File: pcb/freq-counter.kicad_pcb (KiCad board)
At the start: 4 copper layers, 152.4 x 167.6 mm, 107 parts, among them J1 RPM on board, J10 Power_T1, J11 Hz/RPM_Terminal1, J12 Hz/RPM_Terminal0, J13 1kMG_Terminal1, J14 1kMG_Terminal0, J2 BNC, J3 RPM to Board, J4 Jack-DC, J5 Segments-Terminal0, J6 Digits-Terminal0, J7 Segments-Terminal1, J8 Digits-Terminal1, J9 Power_Terminal1, Q1 CSC388A, Q10 2SC1815, Q11 2SC1815, Q12 2SC1815, Q13 2SC1815, Q14 2SC1815, Q2 CSC388A, Q3 2SA1015, Q4 2SC1815, Q5 2SC1815, Q6 CSC388A, Q7 CSC388A, Q8 CSC388A, Q9 2SC1815, SW1 on/off, SW2 count up, SW3 toggle, SW4 SW_SIGNAL, U1 SN74HC02N, U2 ATTINY4313-PU(freq-counter), U3 EE-SX460, U4 74HC00, U5 74HC00, U6 74HC00, U7 7seg-2digit-ca, U8 7seg-2digit-ca, U9 7seg-2digit-ca, Y1 10MHz

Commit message: LED に関してのCvPcbをやり直した。
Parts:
- D1, D10, D2, D3, D4, D5, D6, D7, D8, D9: footprint LEDs:LED_D5.0mm -> LED_THT:LED_D5.0mm

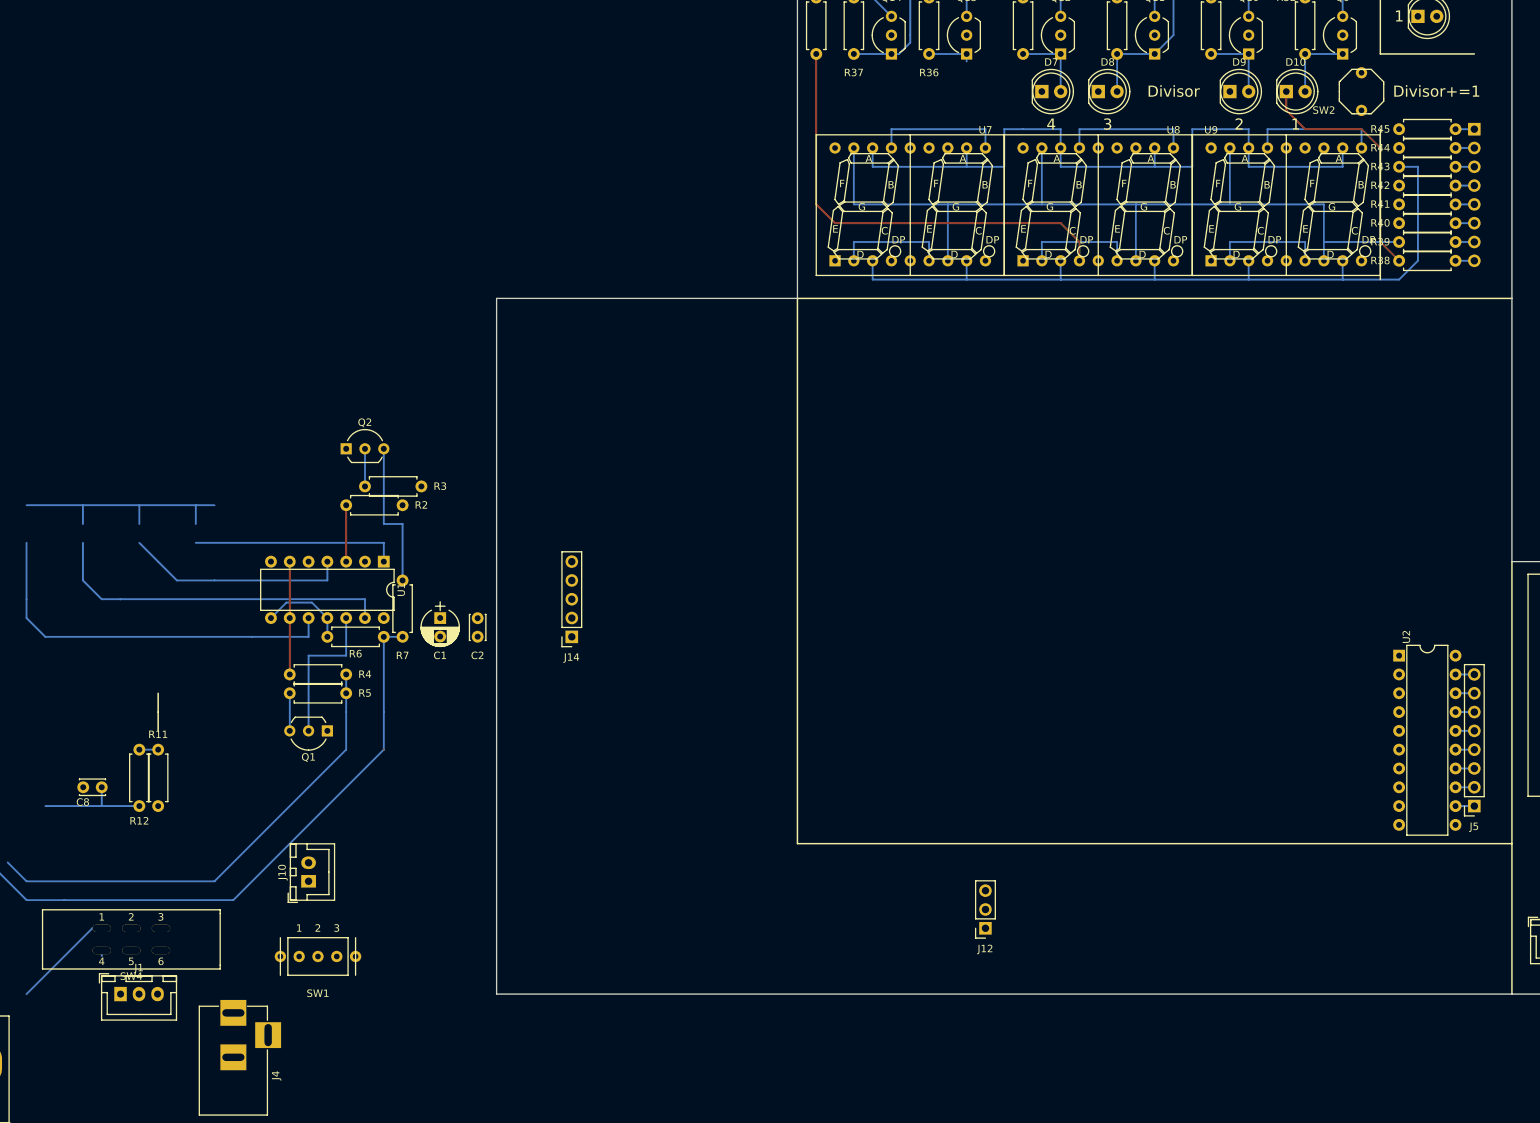
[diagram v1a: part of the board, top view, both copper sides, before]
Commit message: count-up を Terminal 化した。
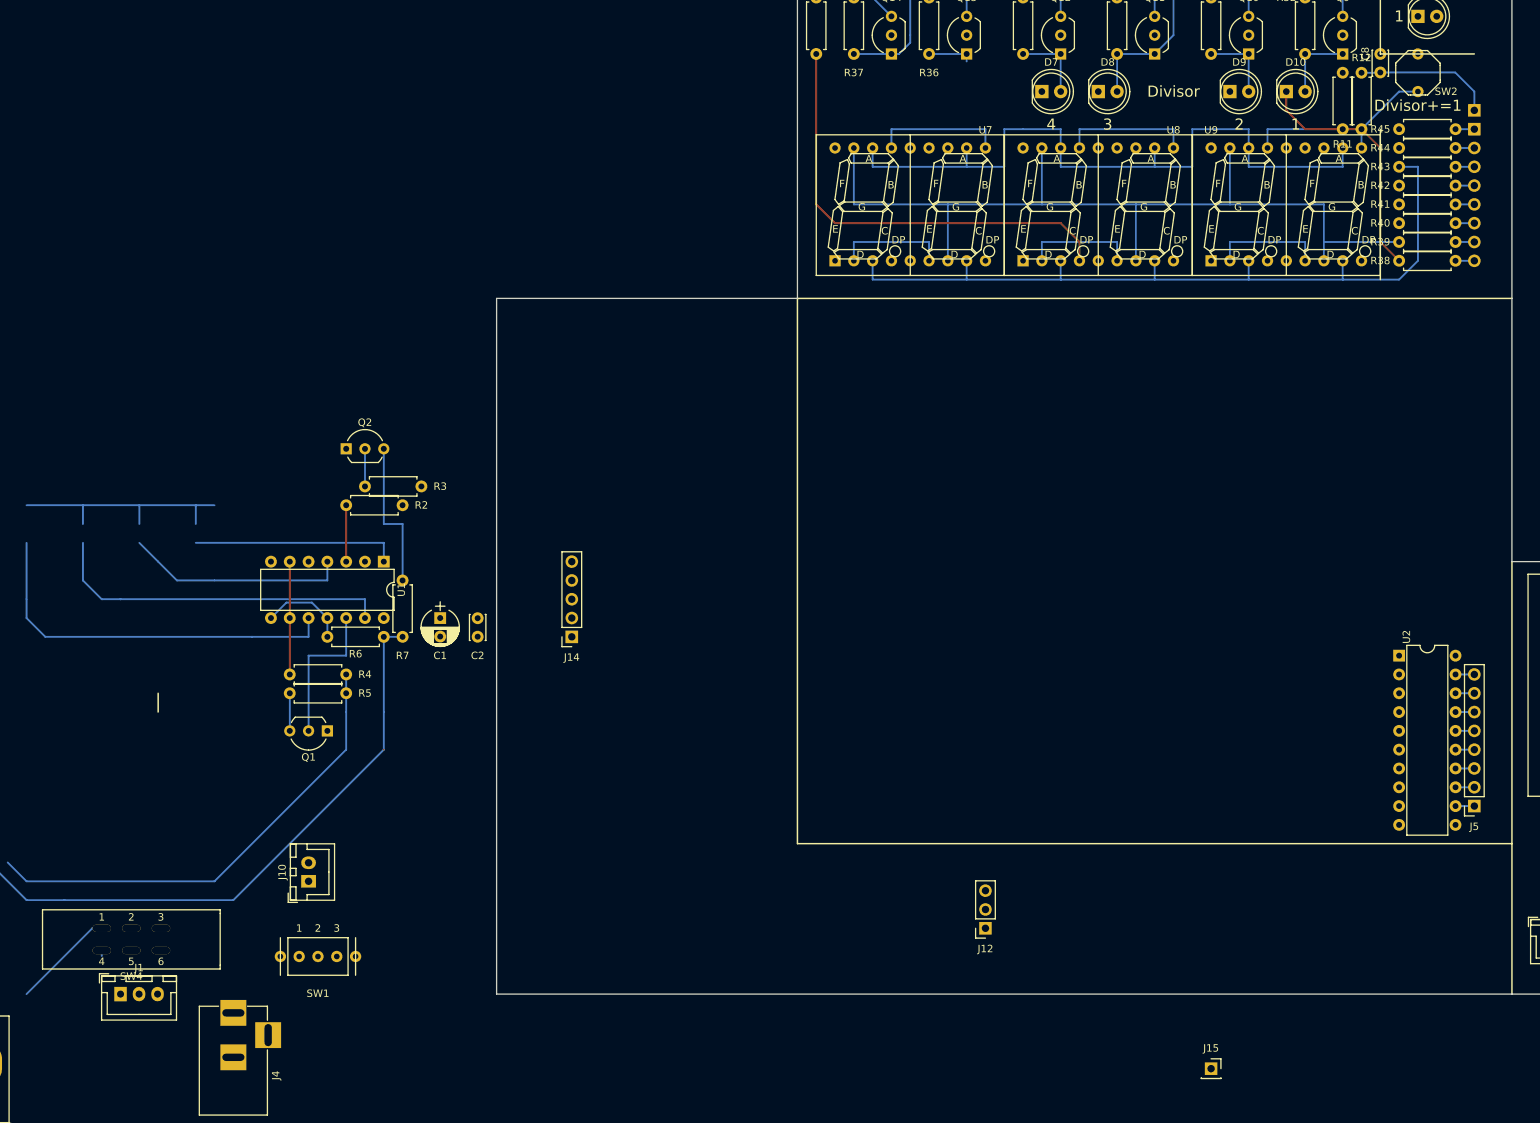
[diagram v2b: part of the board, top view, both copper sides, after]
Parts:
- added J15: count-up_T0, Connector_PinSocket_2.54mm:PinSocket_1x01_P2.54mm_Vertical, F.Cu at (139.7, 208.2)
- added J16: count-up_T1, Connector_PinHeader_2.54mm:PinHeader_1x01_P2.54mm_Vertical, B.Cu at (175.3, 78.7)
- moved C8 201.3 mm to (162.6, 71.1), turned to 270 degrees
- moved R12 192.5 mm to (160.0, 73.7), turned to 270 degrees
- moved R11 180.6 mm to (157.5, 81.3), turned to 90 degrees
- moved SW2 8.03 mm to (167.6, 73.7)
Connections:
- C8 pad 1: VCC -> VCC_T1
- C8 pad 2: /count-up-1-to-4 -> Net-(C8-Pad2)
- R11 pad 2: GND -> GND_T1
- R12 pad 1: /count-up-1-to-4 -> Net-(C8-Pad2)
- SW2 pad 2: VCC -> VCC_T1
- U2 pad 11: /count-up-1-to-4 -> Net-(J15-Pad1)
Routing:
- net Net-(R11-Pad1): track 2.54 -> 52.3 mm
- net /7seg/KDP: track 76.8 -> 49.3 mm
- net Net-(C8-Pad2): track 0.00 -> 18.9 mm
- net /count-up-1-to-4: track 15.2 -> 0.00 mm
- net /7seg/KB: track 52.8 -> 37.7 mm
- net VCC_T1: track 148.4 -> 161.1 mm

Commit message: combine Segments-Terminal? and count-up-Terminal?
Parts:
- removed J15: count-up_T0, Connector_PinSocket_2.54mm:PinSocket_1x01_P2.54mm_Vertical
- removed J16: count-up_T1, Connector_PinHeader_2.54mm:PinHeader_1x01_P2.54mm_Vertical
- J5: footprint Connector_PinSocket_2.54mm:PinSocket_1x08_P2.54mm_Vertical -> Connector_PinSocket_2.54mm:PinSocket_1x09_P2.54mm_Vertical
- J7: footprint Connector_PinHeader_2.54mm:PinHeader_1x08_P2.54mm_Vertical -> Connector_PinHeader_2.54mm:PinHeader_1x09_P2.54mm_Vertical
- Q1, Q10, Q11, Q12, Q13, Q14, Q2, Q3, Q4, Q5, Q6, Q7, Q8, Q9: footprint TO_SOT_Packages_THT:TO-92_Inline_Wide -> Package_TO_SOT_THT:TO-92_Inline_Wide
- moved J7 2.54 mm to (175.3, 78.7)
- moved U2 2.54 mm to (165.1, 149.9)
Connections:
- C8 pad 2: Net-(C8-Pad2) -> /COUNT-UP_T1
- J5 pad 1: Net-(J5-Pad1) -> /COUNT-UP_T0
- J7 pad 1: /7seg/PB0 -> /COUNT-UP_T1
- J7 pad 2: /7seg/PB1 -> /7seg/PB0
- J7 pad 3: /7seg/PB2 -> /7seg/PB1
- J7 pad 4: /7seg/PB3 -> /7seg/PB2
- J7 pad 5: /7seg/PB4 -> /7seg/PB3
- J7 pad 6: /7seg/PB5 -> /7seg/PB4
- J7 pad 7: /7seg/PB6 -> /7seg/PB5
- J7 pad 8: /7seg/PB7 -> /7seg/PB6
- R12 pad 1: Net-(C8-Pad2) -> /COUNT-UP_T1
- U2 pad 11: Net-(J15-Pad1) -> /COUNT-UP_T0
- U2 pad 12: Net-(J5-Pad1) -> Net-(J5-Pad2)
- U2 pad 13: Net-(J5-Pad2) -> Net-(J5-Pad3)
- U2 pad 14: Net-(J5-Pad3) -> Net-(J5-Pad4)
- U2 pad 15: Net-(J5-Pad4) -> Net-(J5-Pad5)
- U2 pad 16: Net-(J5-Pad5) -> Net-(J5-Pad6)
- U2 pad 17: Net-(J5-Pad6) -> Net-(J5-Pad7)
- U2 pad 18: Net-(J5-Pad7) -> Net-(J5-Pad8)
- U2 pad 19: Net-(J5-Pad8) -> Net-(J5-Pad9)
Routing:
- net Net-(C8-Pad2): track 18.9 -> 0.00 mm
- net /COUNT-UP_T1: track 0.00 -> 18.9 mm
- net Net-(R11-Pad1): track 52.3 -> 33.6 mm
- net /7seg/KDP: track 49.3 -> 65.6 mm
- net Net-(J5-Pad9): track 0.00 -> 5.08 mm
- net Net-(J5-Pad1): track 2.54 -> 0.00 mm
- net /7seg/KB: track 37.7 -> 40.1 mm

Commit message: 余分な配線やビヤを削除。その他，不必要となった箇所を削除。
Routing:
- net /1kMG-H: track 81.6 -> 2.54 mm
- net /1kMG-L: track 64.3 -> 2.54 mm
- net /LED_1: track 51.9 -> 0.00 mm
- net (no net): track 61.0 -> 12.7 mm
- net /LED_k: track 46.8 -> 0.00 mm
- net /LED_M: track 30.0 -> 0.00 mm
- net /7seg/KE: track 106.5 -> 76.5 mm
- net /LED_G: track 27.9 -> 0.00 mm
- net Net-(R11-Pad1): track 33.6 -> 9.72 mm
- net /KD24: track 41.2 -> 17.8 mm
- net GND_T1: track 133.8 -> 110.7 mm
- net /7seg/KDP: track 65.6 -> 43.2 mm
- net VCC_T1: track 161.1 -> 140.8 mm
- net /Hz/RPM_T0: track 36.6 -> 18.8 mm
- net /SIGNAL_BNC: track 13.8 -> 0.00 mm
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
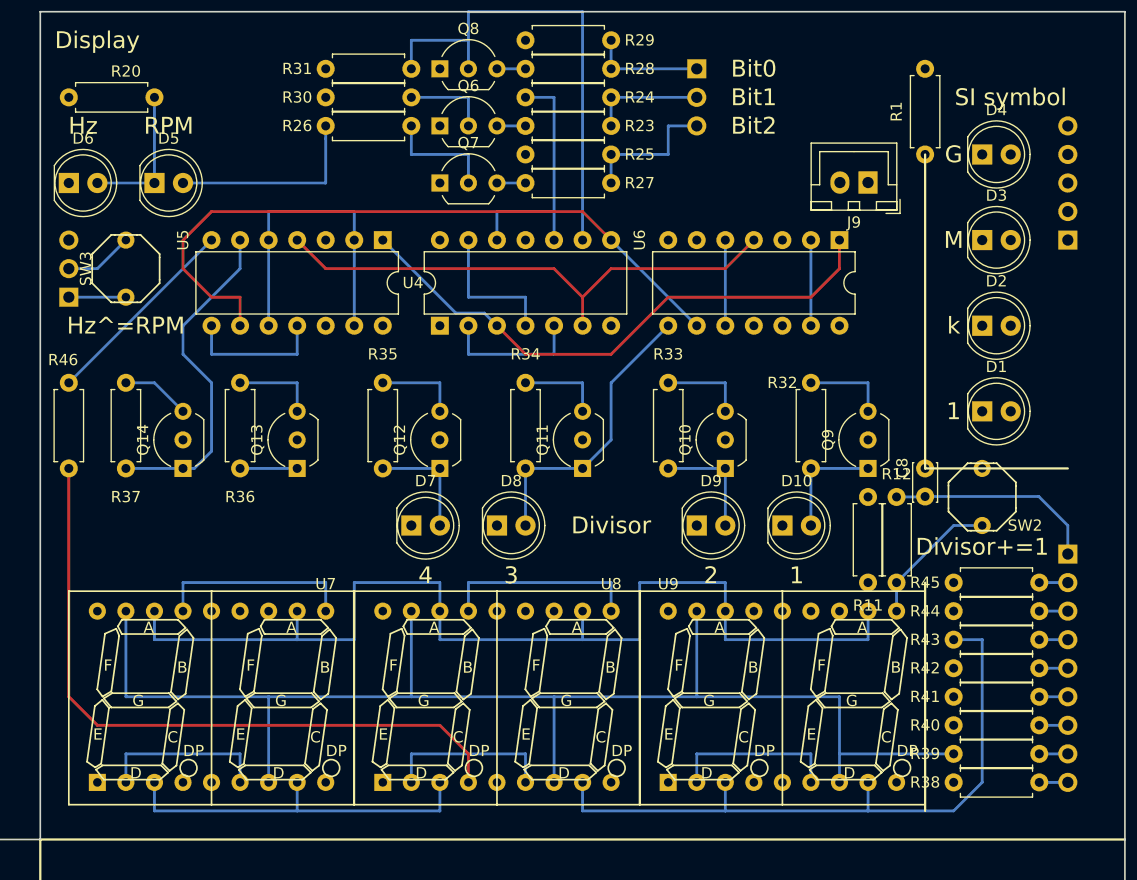
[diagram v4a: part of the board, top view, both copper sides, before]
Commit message: 上階のDisplay部は配線が完了したと考えている。
あとは，上階のPinHeaderに合わせて，下階のPinSocketを配置して配線を頑張るだけ。
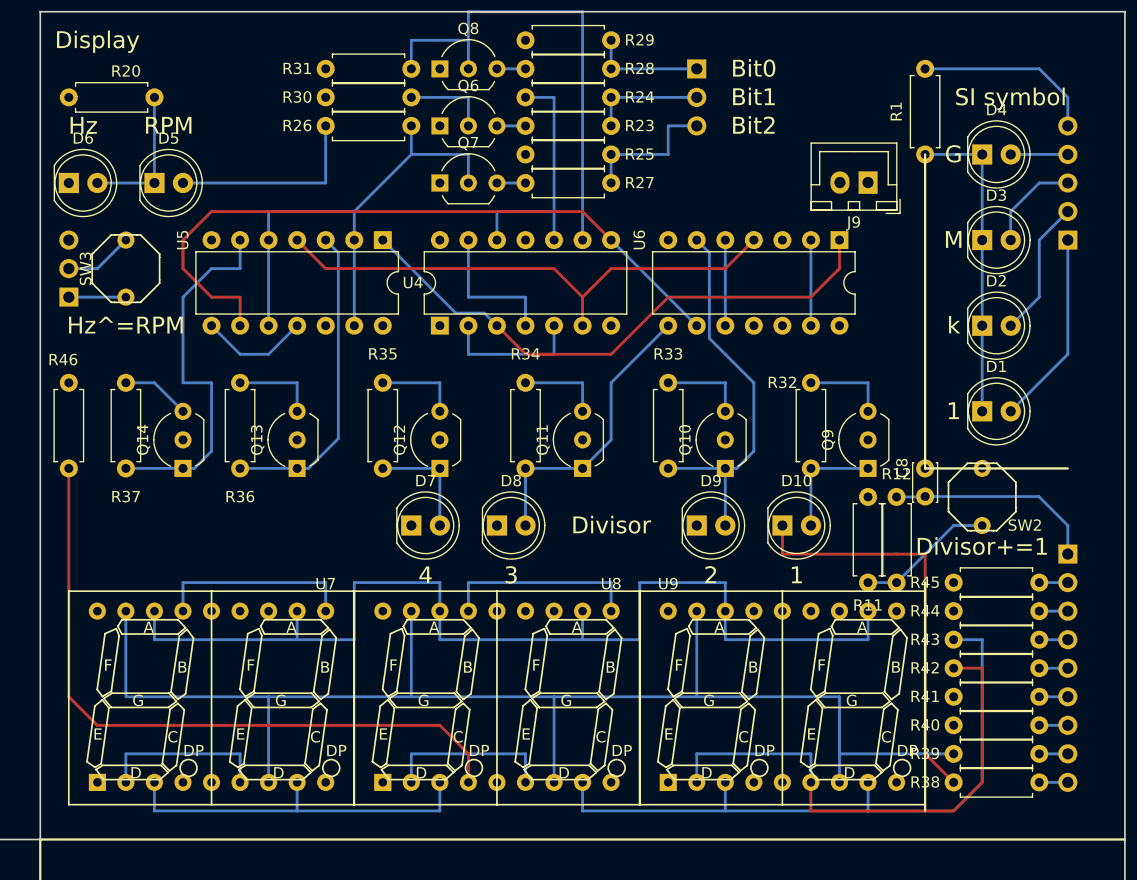
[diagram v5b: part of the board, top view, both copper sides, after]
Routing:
- net GND_T1: track 110.7 -> 188.8 mm
- net /7seg/KDP: track 43.2 -> 79.8 mm
- net /7seg/KF: track 81.3 -> 113.9 mm
- net Net-(D1-Pad1): track 0.00 -> 27.9 mm
- net /KD11: track 19.9 -> 44.0 mm
- net /KD24: track 17.8 -> 40.7 mm
- net VCC_T1: track 140.8 -> 161.1 mm
- net /7seg/KE: track 76.5 -> 95.3 mm
- net Net-(D1-Pad2): track 0.00 -> 17.3 mm
- net Net-(J13-Pad5): track 0.00 -> 16.3 mm
- net /7seg/KD: track 63.6 -> 76.7 mm
- net Net-(D2-Pad2): track 0.00 -> 12.3 mm
- net Net-(D3-Pad2): track 0.00 -> 8.67 mm
- net /7seg/KA: track 98.3 -> 106.0 mm
- net Net-(Q7-Pad2): track 38.1 -> 45.3 mm
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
